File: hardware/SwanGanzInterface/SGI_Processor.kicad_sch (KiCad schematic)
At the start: 0 parts

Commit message: Changed location of lib files, added microcontroller schematic
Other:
- note added: "Processor : CC2340R5"
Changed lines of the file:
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@@
 		(comment 3 "Faculty Mentor - Dr. Valvano")
 	)
+	(text "Processor : CC2340R5"
+		(exclude_from_sim no)
+		(at 49.53 18.415 0)
+		(effects
+			(font
+				(size 3.81 3.81)
+			)
+		)
+	)
 )

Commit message: Closed Kicad
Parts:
- added U7: ~, symbol SGI_SymbolLib:LP-EM-CC2340R5

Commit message: Started msp0 symbol
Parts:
- removed U7: ~, symbol SGI_SymbolLib:LP-EM-CC2340R5
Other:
- note removed: "Processor : CC2340R5"

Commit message: Finished MSP-LP Symbol, Started Pressure_Connector Symbol
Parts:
- added U7: LP-MSPM0G3507, symbol SGI_SymbolLib:LP-MSPM0G3507

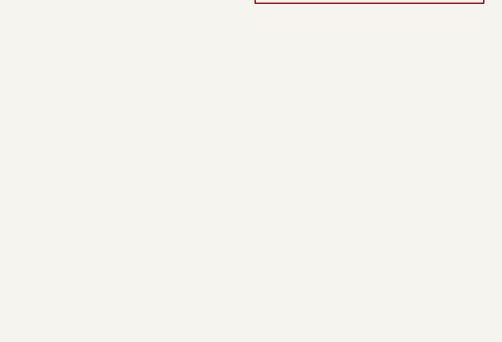
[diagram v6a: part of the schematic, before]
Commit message: Updated gain and added power connector
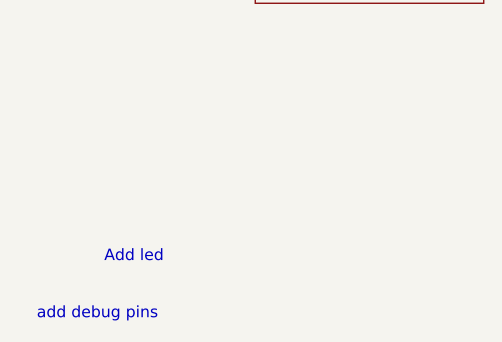
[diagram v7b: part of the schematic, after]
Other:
- note added: "Add led"
- note added: "add debug pins"
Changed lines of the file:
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@@
 		(comment 3 "Faculty Mentor - Dr. Valvano")
+	)
+	(text "add debug pins"
+		(exclude_from_sim no)
+		(at 33.274 158.242 0)
+		(effects
+			(font
+				(size 1.27 1.27)
+			)
+		)
+	)
+	(text "Add led"
+		(exclude_from_sim no)
+		(at 37.338 151.892 0)
+		(effects
+			(font
+				(size 1.27 1.27)
+			)
+		)
 	)
 	(symbol

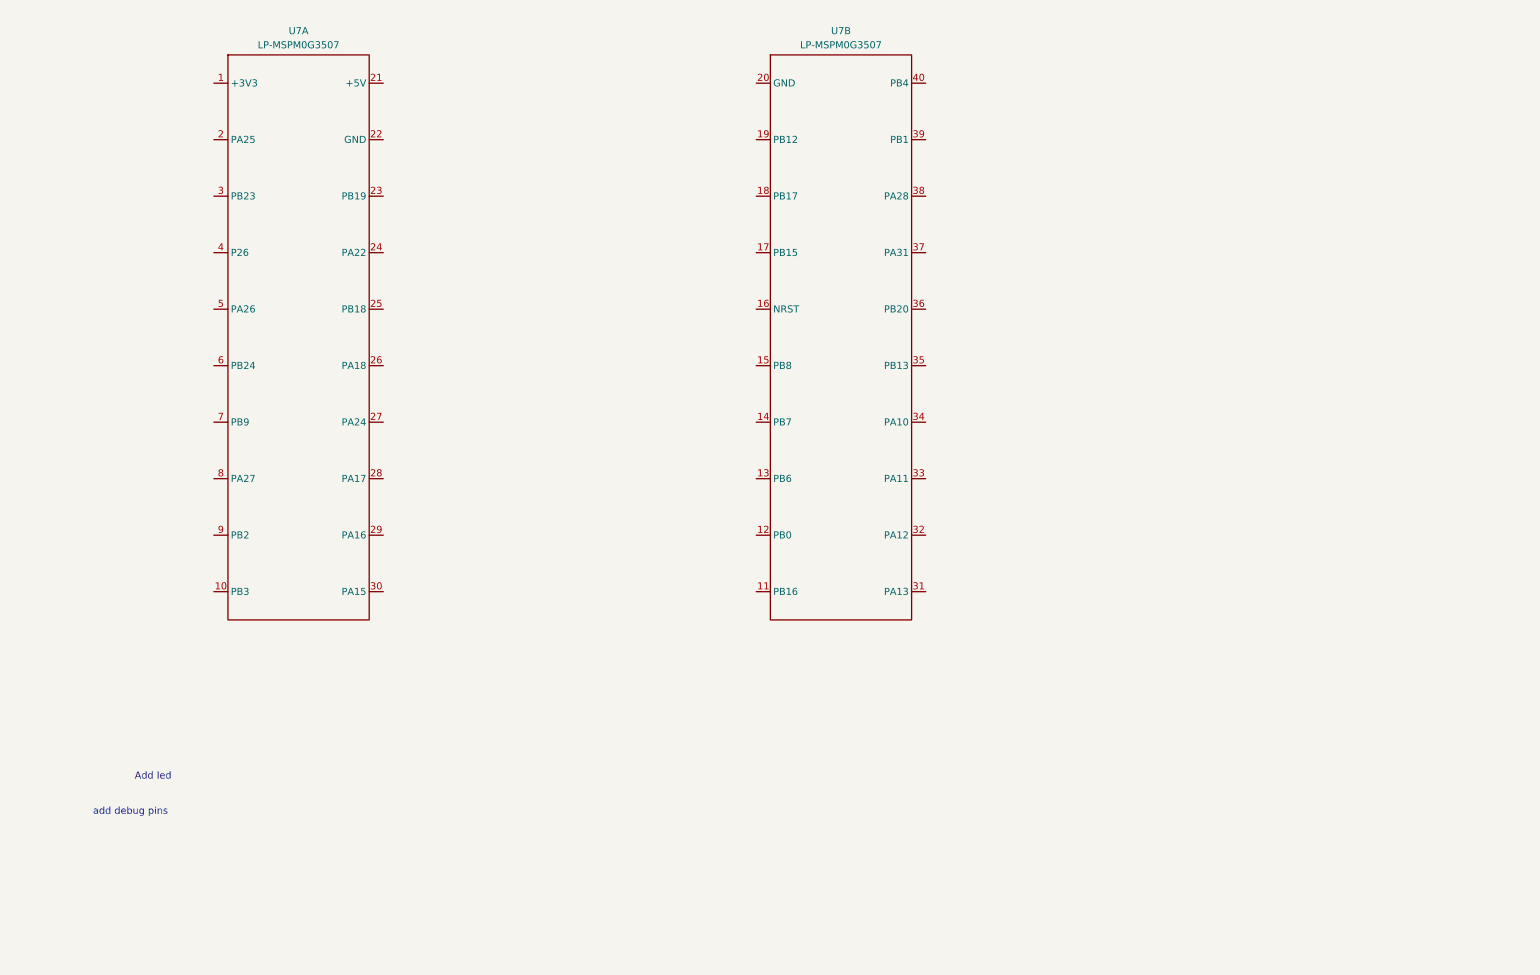
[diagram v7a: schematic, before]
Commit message: Reverse Polarity Fet, Updated Notes, Added second gain stage for pressure, General Updates
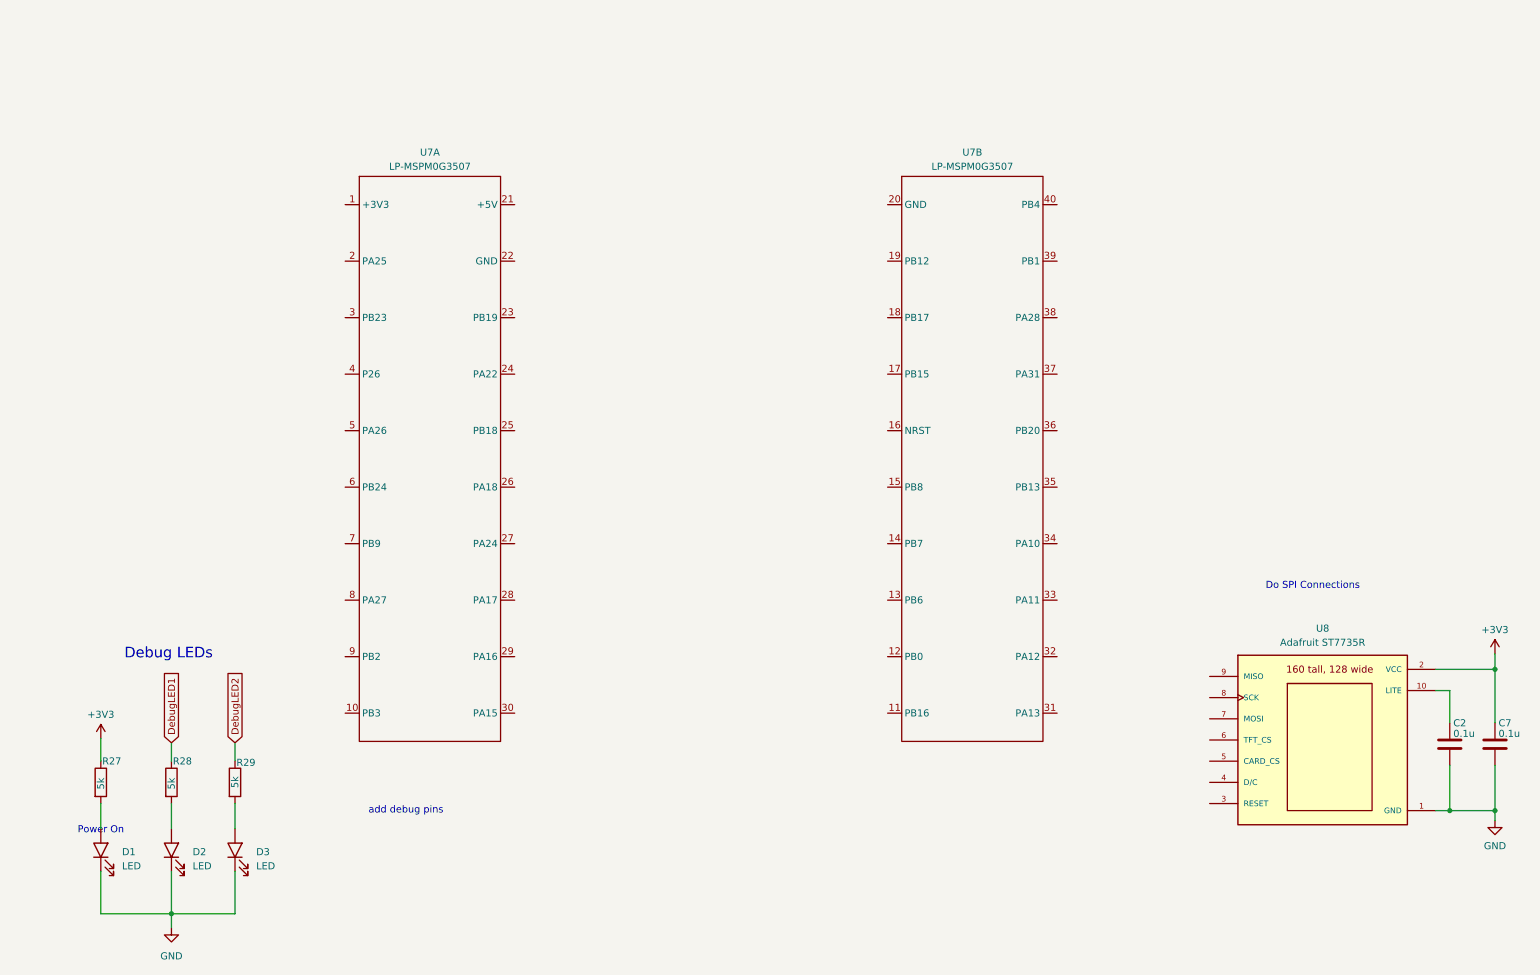
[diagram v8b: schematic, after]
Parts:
- added C2, C7: 0.1u, symbol Device:C
- added D1, D2, D3: LED, SGI_FootprintsLib:LED_D5.0mm, symbol SGI_SymbolLib:LED
- added R27, R28, R29: 5k, symbol Device:R
- added U8: Adafruit ST7735R, SGI_FootprintsLib:adafruit_st7735r, symbol SGI_SymbolLib:Adafruit_ST7735R
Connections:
- new net: D1.2 (A), R27.2
- new net: D1.1 (K), D2.1 (K), D3.1 (K)
- new net: D2.2 (A), R28.2
- new net: D3.2 (A), R29.2
- new net: C2.1, U8.10 (LITE)
- new net +3V3: C7.1, R27.1, U8.2 (VCC)
- new net DebugLED1: R28.1
- new net DebugLED2: R29.1
- new net GND: C2.2, C7.2, U8.1 (GND)
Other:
- note added: "Debug LEDs"
- note added: "Do SPI Connections"
- note added: "Power On"
- note removed: "Add led"
- moved on the sheet: U7A, U7B
